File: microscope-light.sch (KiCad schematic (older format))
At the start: 41 parts, among them J1 USB_C_Receptacle_USB2.0, J2 TagConnect_TC2030_SWD, SW1 WARM, SW2 COLD, SW3 BRIGHT, SW4 DIM, U3 STM32F030F4Px, U4 XC6206PxxxMR

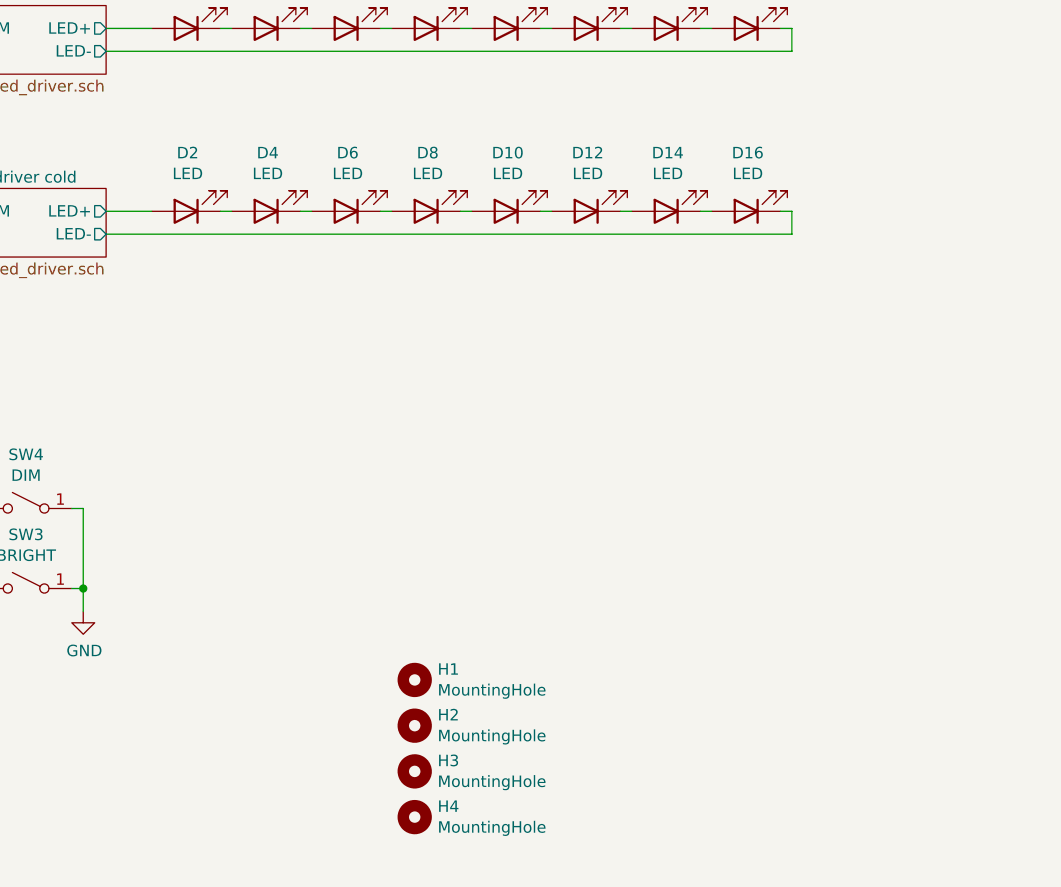
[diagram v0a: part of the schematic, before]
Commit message: Add fabrication features
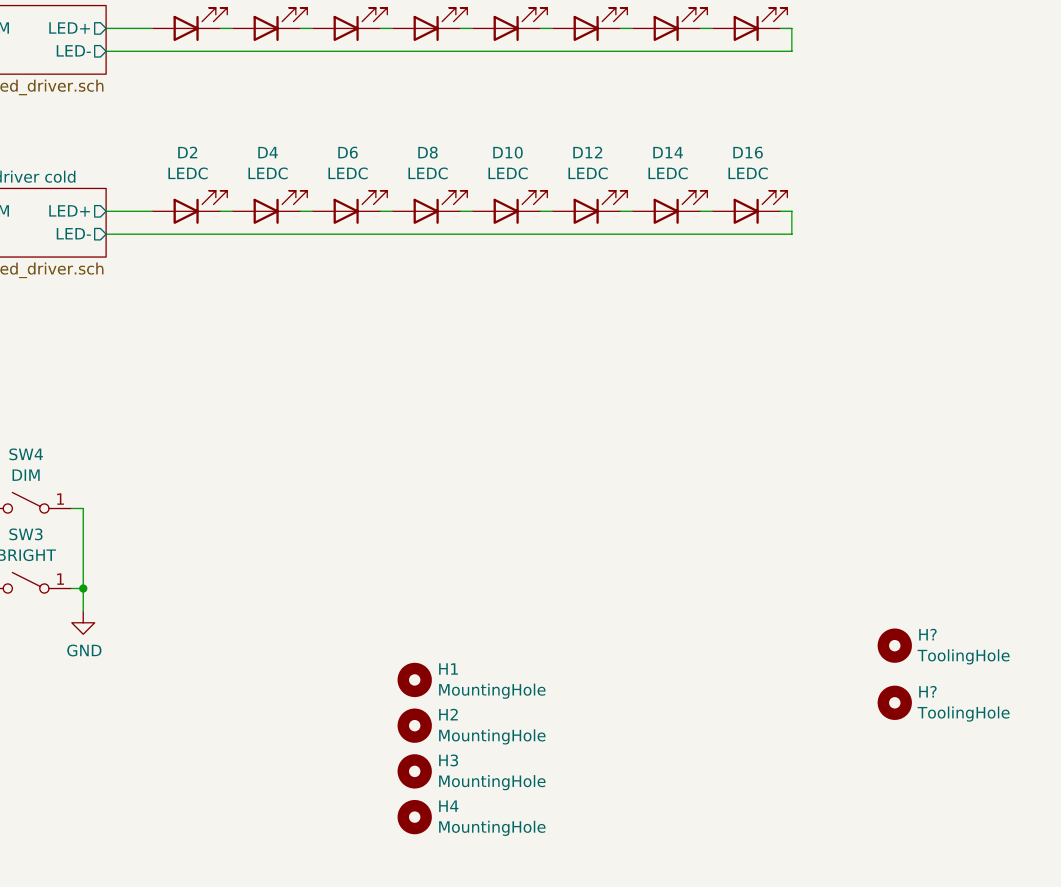
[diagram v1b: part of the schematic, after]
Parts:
- added H? (x2): ToolingHole, ToolingHole:ToolingHole_JLCSMT, symbol Mechanical:MountingHole
- D10, D12, D14, D16, D2, D4, D6, D8: value LED -> LEDC
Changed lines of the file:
@@
 P 6850 3100
 F 0 "D2" H 6843 2845 50  0000 C CNN
-F 1 "LED" H 6843 2936 50  0000 C CNN
+F 1 "LEDC" H 6843 2936 50  0000 C CNN
 F 2 "LED_SMD_HONGLITRONIC:PLCC-2" H 6850 3100 50  0001 C CNN
 F 3 "~" H 6850 3100 50  0001 C CNN
@@
 P 7200 3100
 F 0 "D4" H 7193 2845 50  0000 C CNN
-F 1 "LED" H 7193 2936 50  0000 C CNN
+F 1 "LEDC" H 7193 2936 50  0000 C CNN
 F 2 "LED_SMD_HONGLITRONIC:PLCC-2" H 7200 3100 50  0001 C CNN
 F 3 "~" H 7200 3100 50  0001 C CNN
@@
 P 7550 3100
 F 0 "D6" H 7543 2845 50  0000 C CNN
-F 1 "LED" H 7543 2936 50  0000 C CNN
+F 1 "LEDC" H 7543 2936 50  0000 C CNN
 F 2 "LED_SMD_HONGLITRONIC:PLCC-2" H 7550 3100 50  0001 C CNN
 F 3 "~" H 7550 3100 50  0001 C CNN
@@
 P 7900 3100
 F 0 "D8" H 7893 2845 50  0000 C CNN
-F 1 "LED" H 7893 2936 50  0000 C CNN
+F 1 "LEDC" H 7893 2936 50  0000 C CNN
 F 2 "LED_SMD_HONGLITRONIC:PLCC-2" H 7900 3100 50  0001 C CNN
 F 3 "~" H 7900 3100 50  0001 C CNN
@@
 P 8250 3100
 F 0 "D10" H 8243 2845 50  0000 C CNN
-F 1 "LED" H 8243 2936 50  0000 C CNN
+F 1 "LEDC" H 8243 2936 50  0000 C CNN
 F 2 "LED_SMD_HONGLITRONIC:PLCC-2" H 8250 3100 50  0001 C CNN
 F 3 "~" H 8250 3100 50  0001 C CNN
@@
 P 8600 3100
 F 0 "D12" H 8593 2845 50  0000 C CNN
-F 1 "LED" H 8593 2936 50  0000 C CNN
+F 1 "LEDC" H 8593 2936 50  0000 C CNN
 F 2 "LED_SMD_HONGLITRONIC:PLCC-2" H 8600 3100 50  0001 C CNN
 F 3 "~" H 8600 3100 50  0001 C CNN
@@
 P 8950 3100
 F 0 "D14" H 8943 2845 50  0000 C CNN
-F 1 "LED" H 8943 2936 50  0000 C CNN
+F 1 "LEDC" H 8943 2936 50  0000 C CNN
 F 2 "LED_SMD_HONGLITRONIC:PLCC-2" H 8950 3100 50  0001 C CNN
 F 3 "~" H 8950 3100 50  0001 C CNN
@@
 P 9300 3100
 F 0 "D16" H 9293 2845 50  0000 C CNN
-F 1 "LED" H 9293 2936 50  0000 C CNN
+F 1 "LEDC" H 9293 2936 50  0000 C CNN
 F 2 "LED_SMD_HONGLITRONIC:PLCC-2" H 9300 3100 50  0001 C CNN
 F 3 "~" H 9300 3100 50  0001 C CNN
@@
 	1    0    0    -1
 $EndComp
+$Comp
+L Mechanical:MountingHole H?
+U 1 1 60065CA3
+P 9950 5000
+F 0 "H?" H 10050 5046 50  0000 L CNN
+F 1 "ToolingHole" H 10050 4955 50  0000 L CNN
+F 2 "ToolingHole:ToolingHole_JLCSMT" H 9950 5000 50  0001 C CNN
+F 3 "~" H 9950 5000 50  0001 C CNN
+	1    9950 5000
+	1    0    0    -1
+$EndComp
+$Comp
+L Mechanical:MountingHole H?
+U 1 1 600666BA
+P 9950 5250
+F 0 "H?" H 10050 5296 50  0000 L CNN
+F 1 "ToolingHole" H 10050 5205 50  0000 L CNN
+F 2 "ToolingHole:ToolingHole_JLCSMT" H 9950 5250 50  0001 C CNN
+F 3 "~" H 9950 5250 50  0001 C CNN
+	1    9950 5250
+	1    0    0    -1
+$EndComp

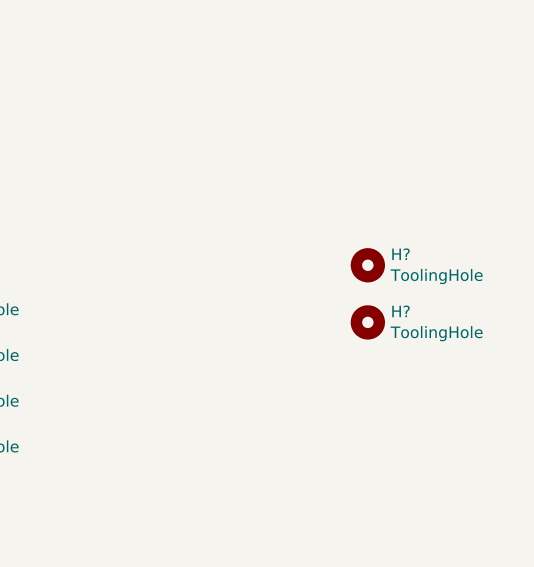
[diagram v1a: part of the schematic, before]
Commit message: Add schematic export
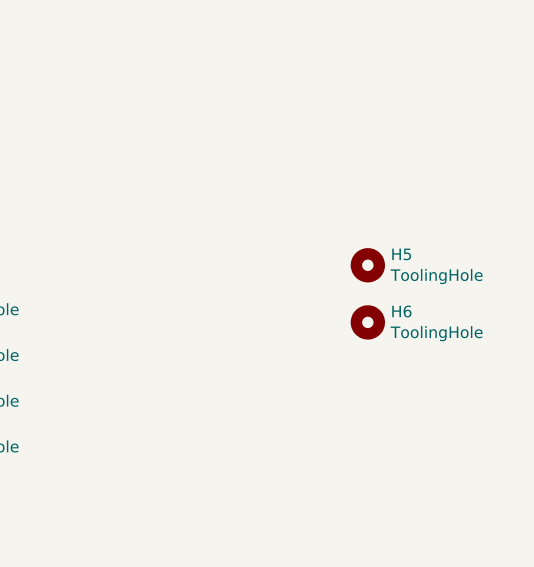
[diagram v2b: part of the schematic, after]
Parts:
- gave numbers to parts that had none: 2
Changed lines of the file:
@@
 encoding utf-8
 Sheet 1 3
-Title ""
-Date ""
-Rev ""
-Comp ""
+Title "ring light"
+Date "2020-12-30"
+Rev "A"
+Comp "Tobias Schramm"
 Comment1 ""
 Comment2 ""
@@
 $EndComp
 $Comp
-L Mechanical:MountingHole H?
+L Mechanical:MountingHole H5
 U 1 1 60065CA3
 P 9950 5000
-F 0 "H?" H 10050 5046 50  0000 L CNN
+F 0 "H5" H 10050 5046 50  0000 L CNN
 F 1 "ToolingHole" H 10050 4955 50  0000 L CNN
 F 2 "ToolingHole:ToolingHole_JLCSMT" H 9950 5000 50  0001 C CNN
@@
 $EndComp
 $Comp
-L Mechanical:MountingHole H?
+L Mechanical:MountingHole H6
 U 1 1 600666BA
 P 9950 5250
-F 0 "H?" H 10050 5296 50  0000 L CNN
+F 0 "H6" H 10050 5296 50  0000 L CNN
 F 1 "ToolingHole" H 10050 5205 50  0000 L CNN
 F 2 "ToolingHole:ToolingHole_JLCSMT" H 9950 5250 50  0001 C CNN
